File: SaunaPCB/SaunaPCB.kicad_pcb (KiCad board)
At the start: 2 copper layers, 190 x 110 mm, 75 parts, among them J201 KL3RM7.62, J202 KL3RM7.62, J203 KL3RM7.62, J204 KL2RM5.08, J205 KL3RM7.62, J206 KL3RM7.62, J301 KL2RM5.08, J302 KL2RM5.08, J303 KL2RM5.08, J304 KL2RM5.08, J305 B4B-ZR, J306 B5B-ZR, K201 RP310024, K202 RP310024, K203 RP310024, K204 RP310024, K205 RP310024, K206 RP310024, K207 RP310024, U201 LHE05-20B24, U202 LM2576T-5, U203 4N25, U204 4N25, U205 4N25, U206 DRV5053, U207 DRV5053, U208 DRV5053, U301 ESP32-DEVKITC, U302 ULN2003

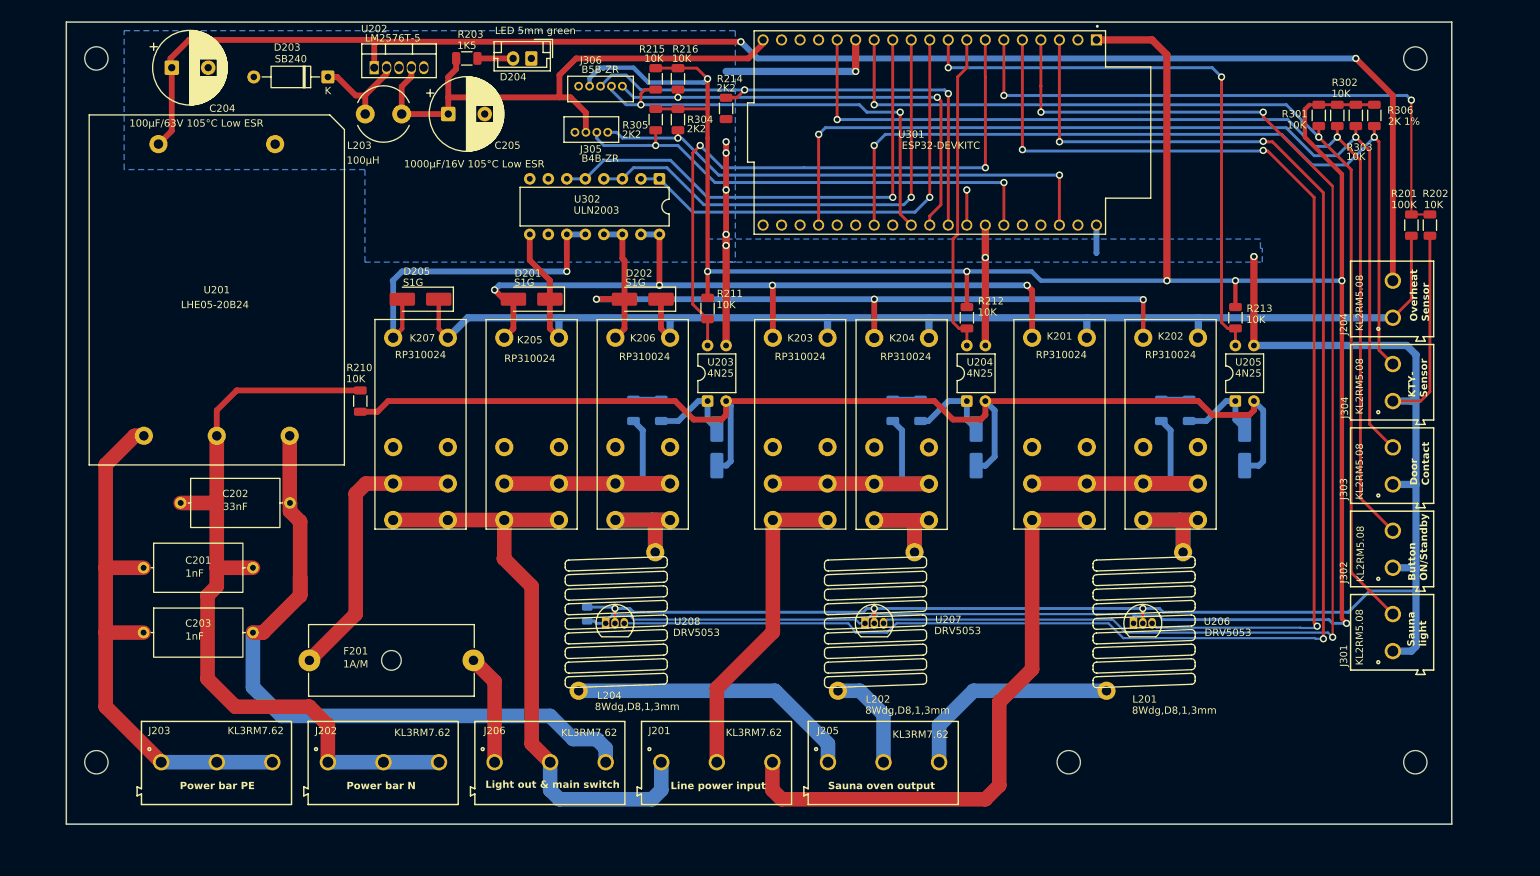
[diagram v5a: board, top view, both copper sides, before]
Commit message: ^MOV and Fuse added
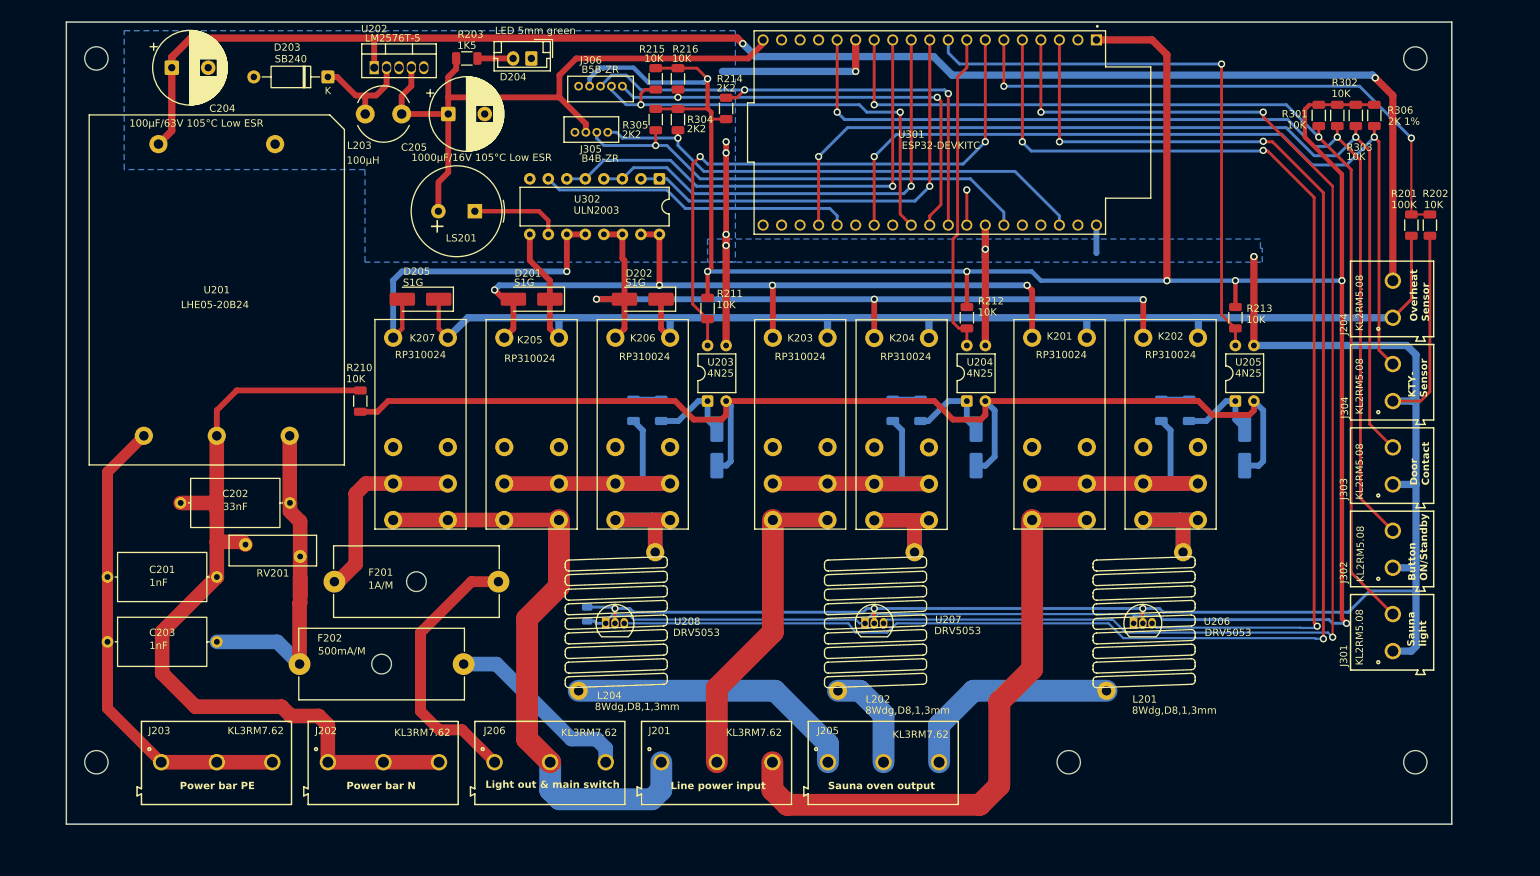
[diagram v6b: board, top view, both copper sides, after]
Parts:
- added F202: 500mA/M, Fuse:Fuseholder_Cylinder-5x20mm_Schurter_0031_8201_Horizontal_Open, F.Cu at (99.0, 130.0)
- added LS201: Speaker_Crystal, Buzzer_Beeper:Buzzer_TDK_PS1240P02BT_D12.2mm_H6.5mm, F.Cu at (123.0, 67.9)
- added RV201: 275V, Varistor:RV_Disc_D12mm_W4.2mm_P7.5mm, F.Cu at (91.6, 113.7)
- moved F201 11.3 mm to (103.8, 118.7)
- moved C201 5.11 mm to (72.6, 118.1)
- moved C203 5.11 mm to (72.6, 127.0)
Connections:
- J206 pad 3: L1_ON -> Net-(F202-Pad2)
- U301 pad 24: unconnected-(U301-IO2-Pad24) -> /Controller part/Summer_3V3
- U302 pad 10: unconnected-(U302-O7-Pad10) -> Net-(U302-O7)
- U302 pad 7: unconnected-(U302-I7-Pad7) -> /Controller part/Summer_3V3
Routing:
- net L1_ON: track 94.9 -> 47.1 mm
- net /Controller part/Summer_3V3: track 0.00 -> 43.0 mm
- net Net-(F202-Pad2): track 0.00 -> 26.2 mm
- net Light_out: track 15.2 -> 37.4 mm
- net +5V: track 77.1 -> 90.1 mm
- net Net-(U302-O7): track 0.00 -> 12.5 mm
- net Net-(F201-Pad1): track 38.7 -> 26.7 mm
- net PE: track 76.5 -> 65.1 mm
- net N: track 107.6 -> 115.0 mm
- net L1_Sense: track 86.6 -> 81.9 mm
- net 24V_FB: track 82.0 -> 78.2 mm
- net SCL: track 72.6 -> 70.0 mm, vias 2 -> 1
- net +3V3: track 391.8 -> 394.2 mm
- net SDA: track 67.2 -> 64.8 mm, vias 2 -> 1
- net /Controller part/R3_3V3: track 69.5 -> 67.3 mm
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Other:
- board text added: "+"

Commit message: Power LED changed to JST connector KTY room added
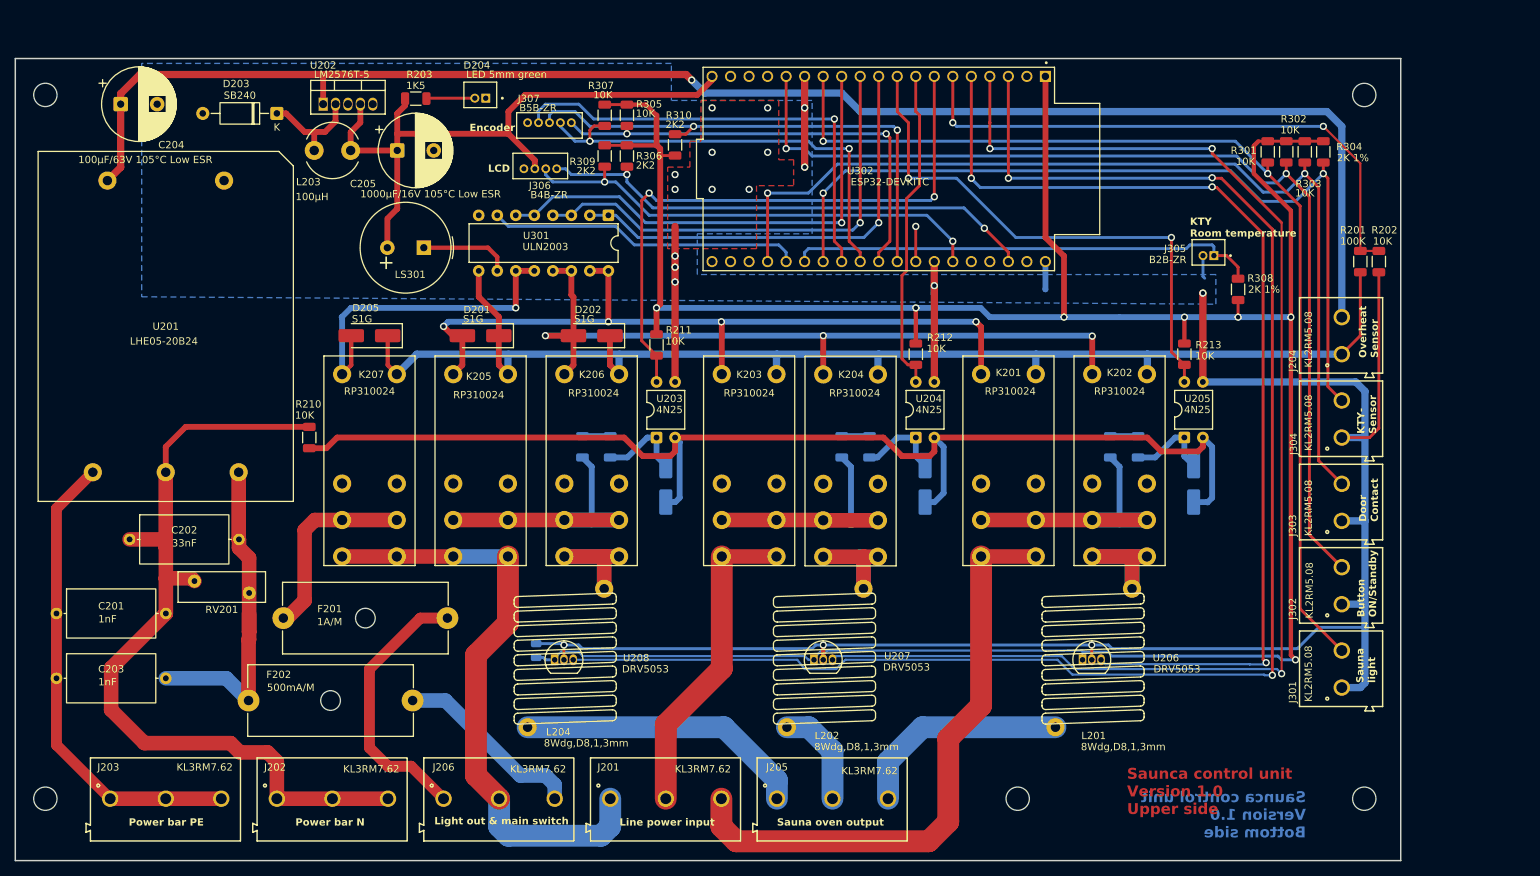
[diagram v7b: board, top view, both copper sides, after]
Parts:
- added J305: B2B-ZR, MyConnectors:B2B-ZR, F.Cu at (223.6, 73.6)
- added R308: 2K 1%, Resistor_SMD:R_1206_3216Metric, F.Cu at (227.7, 78.7)
- D204: footprint Connector_JST:JST_EH_B2B-EH-A_1x02_P2.50mm_Vertical -> MyConnectors:B2B-ZR
- moved R203 8.91 mm to (114.9, 52.5)
- moved D204 8.60 mm to (123.8, 52.0), turned to 0 degrees
- moved L201 8.60 mm to (208.9, 129.5)
- moved L202 8.60 mm to (172.1, 129.5)
- moved L204 8.60 mm to (136.5, 129.5)
- moved U206 8.60 mm to (206.4, 129.5)
- moved U207 8.60 mm to (169.5, 129.5)
- moved U208 8.60 mm to (134.0, 129.5)
- moved C201 8.60 mm to (65.6, 123.1)
- moved C202 8.60 mm to (75.7, 113.0)
- moved C203 8.60 mm to (65.6, 132.0)
- moved C204 8.60 mm to (74.5, 53.3)
- moved C205 8.60 mm to (112.4, 59.6)
- moved C206 8.60 mm to (131.4, 128.2)
- moved D201 8.60 mm to (123.8, 85.0)
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- renumbered J305 to J306, J306 to J307, LS201 to LS301, R306 to R304, R216 to R305, R304 to R306, R215 to R307, R305 to R309, R214 to R310, U302 to U301, U301 to U302
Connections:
- net KTY_Sensor renamed KTY_Oven
- J307 pad 4: +3V3 -> ENC_VCC
- U302 pad 25: unconnected-(U301-IO0-Pad25) -> KTY_Room
- U302 pad 27: unconnected-(U301-IO16-Pad27) -> ENC_VCC
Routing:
- net KTY_Room: track 0.00 -> 64.7 mm
- net ENC_VCC: track 0.00 -> 63.4 mm, vias 0 -> 1
- net +3V3: track 394.2 -> 370.3 mm
- net GND: track 308.6 -> 295.1 mm, vias 10 -> 18
- net L3_Sense: track 79.3 -> 74.6 mm, vias 1 -> 2
- net Net-(D204-A): track 4.89 -> 6.66 mm
- net L1_Sense: track 81.9 -> 83.4 mm
- net 24V_FB: track 78.2 -> 79.1 mm
- net ENC_SWITCH: track 70.4 -> 71.0 mm
- net SDA: track 64.8 -> 65.4 mm, vias 1 -> 2
- net +5V: track 90.1 -> 89.6 mm
- net +24V: track 213.9 -> 214.4 mm, vias 2 -> 1
- net SCL: vias 1 -> 2
- added copper zone on F.Cu, net GND
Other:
- board text added: "0"
- board text added: "0 mm"
- board text added: "0,0000 mm / 0,0000 mm"
- board text added: "0,01 mm"
- board text added: "0,02"
- board text added: "0,035 mm"
- board text added: "0,3000 mm"
- board text added: "1"
- board text added: "1,51 mm"
- board text added: "1,6000 mm"
- board text added: "190,0000 mm x 110,0000 mm"
- board text added: "2"
- board text added: "3,3"
- board text added: "4,5"
- board text added: "Abmessungen der Platine:"
- board text added: "B.Cu"
- board text added: "B.Mask"
- board text added: "B.Paste"
- board text added: "B.Silkscreen"
- board text added: "Bottom Silk Screen"
- board text added: "Bottom Solder Mask"
- board text added: "Bottom Solder Paste"
- board text added: "Castellated Pads:"
- board text added: "Dicke (mm)"
- board text added: "Dielektrikum"
- board text added: "Encoder"
- board text added: "Epsilon R"
- board text added: "F.Cu"
- board text added: "F.Mask"
- board text added: "F.Paste"
- board text added: "F.Silkscreen"
- board text added: "FR4"
- board text added: "Farbe"
- board text added: "HAL lead-free"
- board text added: "Impedanzkontrolle:"
- board text added: "KTY Room temperature"
- board text added: "Kupferlagenanzahl:"
- board text added: "Kupferoberfläche:"
- board text added: "LCD"
- board text added: "Lagenname"
- board text added: "Material"
- board text added: "Metallisierte Platinenkante:"
- board text added: "Min Leiterbahn/abstand:"
- board text added: "Min Lochdurchmesser:"
- board text added: "Nein"
- board text added: "Not specified"
- board text added: "PLATINEN-EIGENSCHAFTEN"
- board text added: "Platinen-Dicke:"
- board text added: "Randsteckverbinder:"
- board text added: "Saunca control unit Version 1.0 Bottom side"
- board text added: "Saunca control unit Version 1.0 Upper side"
- board text added: "Tangens des Verlustwinkels"
- board text added: "Top Silk Screen"
- board text added: "Top Solder Mask"
- board text added: "Top Solder Paste"
- board text added: "Typ"
- board text added: "copper"
- board text added: "core"
